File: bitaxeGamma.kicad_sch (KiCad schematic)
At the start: 20 parts, among them J1 54-00164

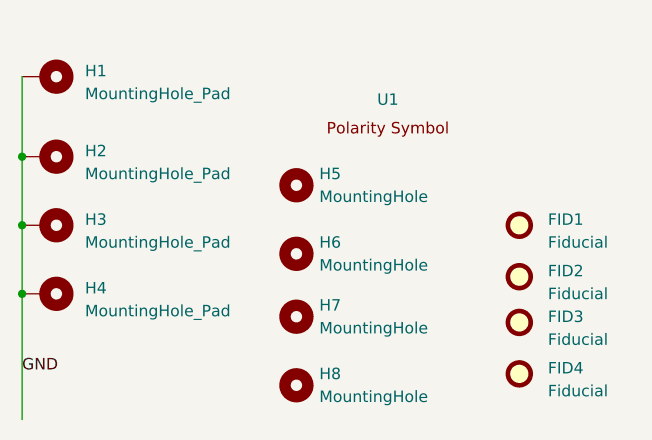
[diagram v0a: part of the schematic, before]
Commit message: switched heatsink mounting holes to all plated M3 (3.2mm) holes, on 41.35mm square pattern. removed thermals from all mounting holes
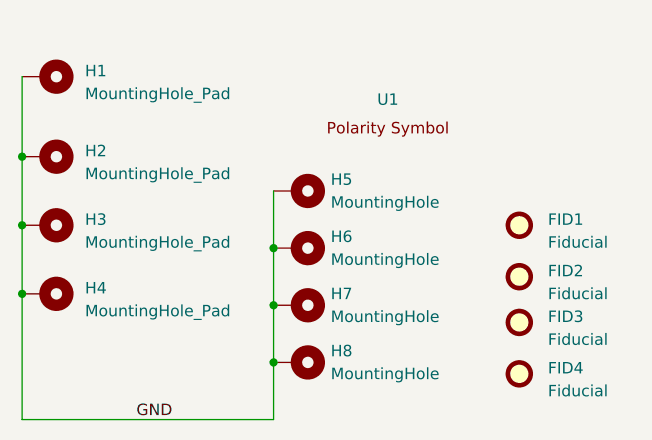
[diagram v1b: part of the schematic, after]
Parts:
- H5, H6: footprint bitaxe:HeatsinkMountingHole_3mm -> MountingHole:MountingHole_3.2mm_M3_Pad; symbol Mechanical:MountingHole -> Mechanical:MountingHole_Pad
- H7: footprint MountingHole:MountingHole_3.5mm -> MountingHole:MountingHole_3.2mm_M3_Pad; symbol Mechanical:MountingHole -> Mechanical:MountingHole_Pad
- H8: footprint bitaxe:HeatsinkMountingHole_3.5mm -> MountingHole:MountingHole_3.2mm_M3_Pad; symbol Mechanical:MountingHole -> Mechanical:MountingHole_Pad
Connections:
- net GND: now also H5.1, H6.1, H7.1, H8.1
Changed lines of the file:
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@@
+	)
+	(junction
+		(at 63.5 186.69)
+		(diameter 0)
+		(color 0 0 0 0)
 	)
 	(junction
@@
 	)
 	(junction
+		(at 63.5 180.34)
+		(diameter 0)
+		(color 0 0 0 0)
+	)
+	(junction
+		(at 63.5 173.99)
+		(diameter 0)
+		(color 0 0 0 0)
+	)
+	(junction
 		(at 35.56 163.83)
 		(diameter 0)
@@
 	(wire
 		(pts
+			(xy 63.5 167.64) (xy 63.5 173.99)
+		)
+		(stroke
+			(width 0)
+			(type default)
+		)
+	)
+	(wire
+		(pts
 			(xy 147.32 74.93) (xy 147.32 69.85)
 		)
@@
 	(wire
 		(pts
+			(xy 63.5 173.99) (xy 63.5 180.34)
+		)
+		(stroke
+			(width 0)
+			(type default)
+		)
+	)
+	(wire
+		(pts
 			(xy 72.39 43.18) (xy 80.01 43.18)
 		)
@@
 	(wire
 		(pts
+			(xy 63.5 186.69) (xy 63.5 193.04)
+		)
+		(stroke
+			(width 0)
+			(type default)
+		)
+	)
+	(wire
+		(pts
 			(xy 167.64 110.49) (xy 175.26 110.49)
 		)
@@
 	(wire
 		(pts
+			(xy 63.5 180.34) (xy 63.5 186.69)
+		)
+		(stroke
+			(width 0)
+			(type default)
+		)
+	)
+	(wire
+		(pts
 			(xy 209.55 49.53) (xy 209.55 69.85)
 		)
@@
 		(pts
 			(xy 147.32 69.85) (xy 175.26 69.85)
+		)
+		(stroke
+			(width 0)
+			(type default)
+		)
+	)
+	(wire
+		(pts
+			(xy 35.56 193.04) (xy 63.5 193.04)
 		)
 		(stroke
@@
 	)
 	(label "GND"
-		(at 35.56 187.96 0)
+		(at 48.26 193.04 0)
 		(fields_autoplaced yes)
 		(effects
@@
 	)
 	(symbol
-		(lib_id "Mechanical:MountingHole")
-		(at 66.04 189.23 0)
+		(lib_name "MountingHole_Pad_4")
+		(lib_id "Mechanical:MountingHole_Pad")
+		(at 66.04 186.69 270)
 		(unit 1)
-		(exclude_from_sim no)
+		(exclude_from_sim yes)
 		(in_bom no)
 		(on_board yes)
@@
 		(fields_autoplaced yes)
 		(property "Reference" "H8"
-			(at 68.58 187.9599 0)
+			(at 69.85 185.4199 90)
 			(effects
 				(font
@@
 		)
 		(property "Value" "MountingHole"
-			(at 68.58 190.4999 0)
-			(effects
-				(font
-					(size 1.27 1.27)
-				)
-				(justify left)
-			)
-		)
-		(property "Footprint" "bitaxe:HeatsinkMountingHole_3.5mm"
-			(at 66.04 189.23 0)
+			(at 69.85 187.9599 90)
+			(effects
+				(font
+					(size 1.27 1.27)
+				)
+				(justify left)
+			)
+		)
+		(property "Footprint" "MountingHole:MountingHole_3.2mm_M3_Pad"
+			(at 66.04 186.69 0)
 			(effects
 				(font
@@
 		)
 		(property "Datasheet" "~"
-			(at 66.04 189.23 0)
-			(effects
-				(font
-					(size 1.27 1.27)
-				)
-				(hide yes)
-			)
-		)
-		(property "Description" ""
-			(at 66.04 189.23 0)
-			(effects
-				(font
-					(size 1.27 1.27)
-				)
-				(hide yes)
-			)
+			(at 66.04 186.69 0)
+			(effects
+				(font
+					(size 1.27 1.27)
+				)
+				(hide yes)
+			)
+		)
+		(property "Description" "Mounting Hole with connection"
+			(at 66.04 186.69 0)
+			(effects
+				(font
+					(size 1.27 1.27)
+				)
+				(hide yes)
+			)
+		)
+		(pin "1"
 		)
 		(instances
@@
 	)
 	(symbol
-		(lib_id "Mechanical:MountingHole")
-		(at 66.04 181.61 0)
+		(lib_name "MountingHole_Pad_3")
+		(lib_id "Mechanical:MountingHole_Pad")
+		(at 66.04 180.34 270)
 		(unit 1)
-		(exclude_from_sim no)
+		(exclude_from_sim yes)
 		(in_bom no)
 		(on_board yes)
@@
 		(fields_autoplaced yes)
 		(property "Reference" "H7"
-			(at 68.58 180.3399 0)
+			(at 69.85 179.0699 90)
 			(effects
 				(font
@@
 		)
 		(property "Value" "MountingHole"
-			(at 68.58 182.8799 0)
-			(effects
-				(font
-					(size 1.27 1.27)
-				)
-				(justify left)
-			)
-		)
-		(property "Footprint" "MountingHole:MountingHole_3.5mm"
-			(at 66.04 181.61 0)
+			(at 69.85 181.6099 90)
+			(effects
+				(font
+					(size 1.27 1.27)
+				)
+				(justify left)
+			)
+		)
+		(property "Footprint" "MountingHole:MountingHole_3.2mm_M3_Pad"
+			(at 66.04 180.34 0)
 			(effects
 				(font
@@
 		)
 		(property "Datasheet" "~"
-			(at 66.04 181.61 0)
-			(effects
-				(font
-					(size 1.27 1.27)
-				)
-				(hide yes)
-			)
-		)
-		(property "Description" ""
-			(at 66.04 181.61 0)
-			(effects
-				(font
-					(size 1.27 1.27)
-				)
-				(hide yes)
-			)
+			(at 66.04 180.34 0)
+			(effects
+				(font
+					(size 1.27 1.27)
+				)
+				(hide yes)
+			)
+		)
+		(property "Description" "Mounting Hole with connection"
+			(at 66.04 180.34 0)
+			(effects
+				(font
+					(size 1.27 1.27)
+				)
+				(hide yes)
+			)
+		)
+		(pin "1"
 		)
 		(instances
@@
 	)
 	(symbol
-		(lib_id "Mechanical:MountingHole")
-		(at 66.04 174.625 0)
+		(lib_name "MountingHole_Pad_2")
+		(lib_id "Mechanical:MountingHole_Pad")
+		(at 66.04 173.99 270)
 		(unit 1)
-		(exclude_from_sim no)
+		(exclude_from_sim yes)
 		(in_bom no)
 		(on_board yes)
@@
 		(fields_autoplaced yes)
 		(property "Reference" "H6"
-			(at 68.58 173.3549 0)
+			(at 69.85 172.7199 90)
 			(effects
 				(font
@@
 		)
 		(property "Value" "MountingHole"
-			(at 68.58 175.8949 0)
-			(effects
-				(font
-					(size 1.27 1.27)
-				)
-				(justify left)
-			)
-		)
-		(property "Footprint" "bitaxe:HeatsinkMountingHole_3mm"
-			(at 66.04 174.625 0)
+			(at 69.85 175.2599 90)
+			(effects
+				(font
+					(size 1.27 1.27)
+				)
+				(justify left)
+			)
+		)
+		(property "Footprint" "MountingHole:MountingHole_3.2mm_M3_Pad"
+			(at 66.04 173.99 0)
 			(effects
 				(font
@@
 		)
 		(property "Datasheet" "~"
-			(at 66.04 174.625 0)
-			(effects
-				(font
-					(size 1.27 1.27)
-				)
-				(hide yes)
-			)
-		)
-		(property "Description" ""
-			(at 66.04 174.625 0)
-			(effects
-				(font
-					(size 1.27 1.27)
-				)
-				(hide yes)
-			)
+			(at 66.04 173.99 0)
+			(effects
+				(font
+					(size 1.27 1.27)
+				)
+				(hide yes)
+			)
+		)
+		(property "Description" "Mounting Hole with connection"
+			(at 66.04 173.99 0)
+			(effects
+				(font
+					(size 1.27 1.27)
+				)
+				(hide yes)
+			)
+		)
+		(pin "1"
 		)
 		(instances
@@
 	)
 	(symbol
-		(lib_id "Mechanical:MountingHole")
-		(at 66.04 167.005 0)
+		(lib_name "MountingHole_Pad_1")
+		(lib_id "Mechanical:MountingHole_Pad")
+		(at 66.04 167.64 270)
 		(unit 1)
-		(exclude_from_sim no)
+		(exclude_from_sim yes)
 		(in_bom no)
 		(on_board yes)
@@
 		(fields_autoplaced yes)
 		(property "Reference" "H5"
-			(at 68.58 165.7349 0)
+			(at 69.85 166.3699 90)
 			(effects
 				(font
@@
 		)
 		(property "Value" "MountingHole"
-			(at 68.58 168.2749 0)
-			(effects
-				(font
-					(size 1.27 1.27)
-				)
-				(justify left)
-			)
-		)
-		(property "Footprint" "bitaxe:HeatsinkMountingHole_3mm"
-			(at 66.04 167.005 0)
+			(at 69.85 168.9099 90)
+			(effects
+				(font
+					(size 1.27 1.27)
+				)
+				(justify left)
+			)
+		)
+		(property "Footprint" "MountingHole:MountingHole_3.2mm_M3_Pad"
+			(at 66.04 167.64 0)
 			(effects
 				(font
@@
 		)
 		(property "Datasheet" "~"
-			(at 66.04 167.005 0)
-			(effects
-				(font
-					(size 1.27 1.27)
-				)
-				(hide yes)
-			)
-		)
-		(property "Description" ""
-			(at 66.04 167.005 0)
-			(effects
-				(font
-					(size 1.27 1.27)
-				)
-				(hide yes)
-			)
+			(at 66.04 167.64 0)
+			(effects
+				(font
+					(size 1.27 1.27)
+				)
+				(hide yes)
+			)
+		)
+		(property "Description" "Mounting Hole with connection"
+			(at 66.04 167.64 0)
+			(effects
+				(font
+					(size 1.27 1.27)
+				)
+				(hide yes)
+			)
+		)
+		(pin "1"
 		)
 		(instances
